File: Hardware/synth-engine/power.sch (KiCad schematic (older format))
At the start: 9 parts

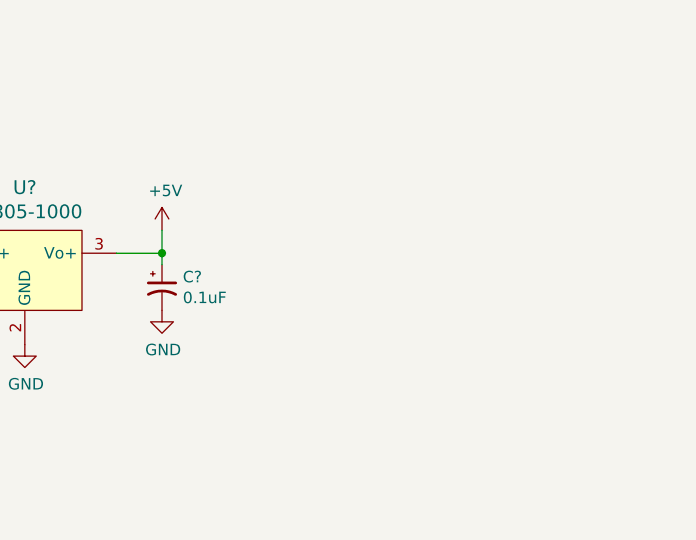
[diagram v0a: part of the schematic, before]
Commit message: add 3.3V voltage regulator
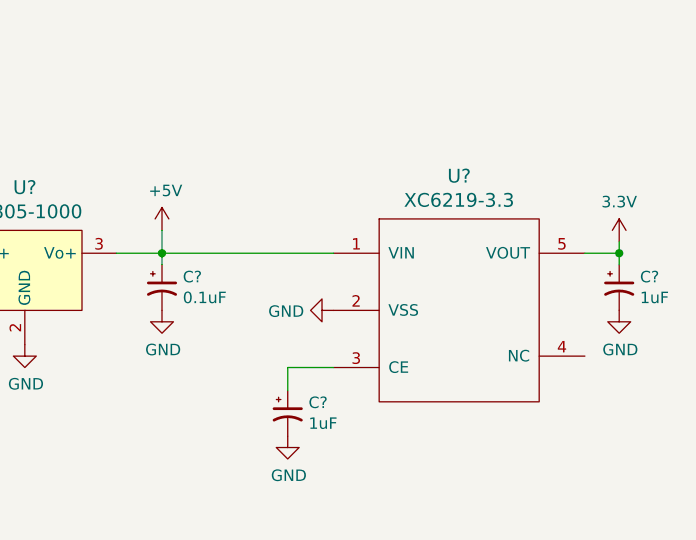
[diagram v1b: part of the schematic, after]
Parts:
- added C? (x2): 1uF, symbol Device:CP1_Small
- added U?: XC6219-3.3, symbol dac:XC6219-3.3
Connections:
- net +5V: now also U?.1 (VIN)
- net GND: now also C?.2, C?.2, U?.2 (VSS)
- new net: C?.1, U?.3 (CE)
- new net 3.3V: C?.1, U?.5 (VOUT)
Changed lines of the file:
@@
 	6150 2100 6150 2200
 Connection ~ 6150 2200
+$Comp
+L SparkFun-Aesthetics:3.3V #SUPPLY?
+U 1 1 5DD89EE3
+P 8150 2150
+F 0 "#SUPPLY?" H 8150 2150 50  0001 L BNN
+F 1 "3.3V" H 8150 2324 50  0000 C CNN
+F 2 "" H 8150 2150 50  0001 C CNN
+F 3 "" H 8150 2150 50  0001 C CNN
+	1    8150 2150
+	1    0    0    -1
+$EndComp
+$Comp
+L dac:XC6219-3.3 U?
+U 1 1 5DD89FB2
+P 7500 2450
+F 0 "U?" H 7450 3037 60  0000 C CNN
+F 1 "XC6219-3.3" H 7450 2931 60  0000 C CNN
+F 2 "" H 7500 2650 60  0000 C CNN
+F 3 "" H 7500 2650 60  0000 C CNN
+	1    7500 2450
+	1    0    0    -1
+$EndComp
+Wire Wire Line
+	6150 2200 6900 2200
+Wire Wire Line
+	8150 2150 8150 2200
+Wire Wire Line
+	8150 2200 8000 2200
+$Comp
+L Device:CP1_Small C?
+U 1 1 5DD8B50D
+P 6700 2900
+F 0 "C?" H 6791 2946 50  0000 L CNN
+F 1 "1uF" H 6791 2855 50  0000 L CNN
+F 2 "" H 6700 2900 50  0001 C CNN
+F 3 "~" H 6700 2900 50  0001 C CNN
+	1    6700 2900
+	1    0    0    -1
+$EndComp
+Wire Wire Line
+	6700 2800 6700 2700
+Wire Wire Line
+	6700 2700 6900 2700
+$Comp
+L power:GND #PWR?
+U 1 1 5DD8B762
+P 6700 3000
+F 0 "#PWR?" H 6700 2750 50  0001 C CNN
+F 1 "GND" H 6705 2827 50  0000 C CNN
+F 2 "" H 6700 3000 50  0001 C CNN
+F 3 "" H 6700 3000 50  0001 C CNN
+	1    6700 3000
+	1    0    0    -1
+$EndComp
+$Comp
+L power:GND #PWR?
+U 1 1 5DD8B7B9
+P 6900 2450
+F 0 "#PWR?" H 6900 2200 50  0001 C CNN
+F 1 "GND" V 6905 2322 50  0000 R CNN
+F 2 "" H 6900 2450 50  0001 C CNN
+F 3 "" H 6900 2450 50  0001 C CNN
+	1    6900 2450
+	0    1    1    0
+$EndComp
+$Comp
+L Device:CP1_Small C?
+U 1 1 5DD8B7E5
+P 8150 2350
+F 0 "C?" H 8241 2396 50  0000 L CNN
+F 1 "1uF" H 8241 2305 50  0000 L CNN
+F 2 "" H 8150 2350 50  0001 C CNN
+F 3 "~" H 8150 2350 50  0001 C CNN
+	1    8150 2350
+	1    0    0    -1
+$EndComp
+Wire Wire Line
+	8150 2250 8150 2200
+Connection ~ 8150 2200
+$Comp
+L power:GND #PWR?
+U 1 1 5DD8BD69
+P 8150 2450
+F 0 "#PWR?" H 8150 2200 50  0001 C CNN
+F 1 "GND" H 8155 2277 50  0000 C CNN
+F 2 "" H 8150 2450 50  0001 C CNN
+F 3 "" H 8150 2450 50  0001 C CNN
+	1    8150 2450
+	1    0    0    -1
+$EndComp
 $EndSCHEMATC

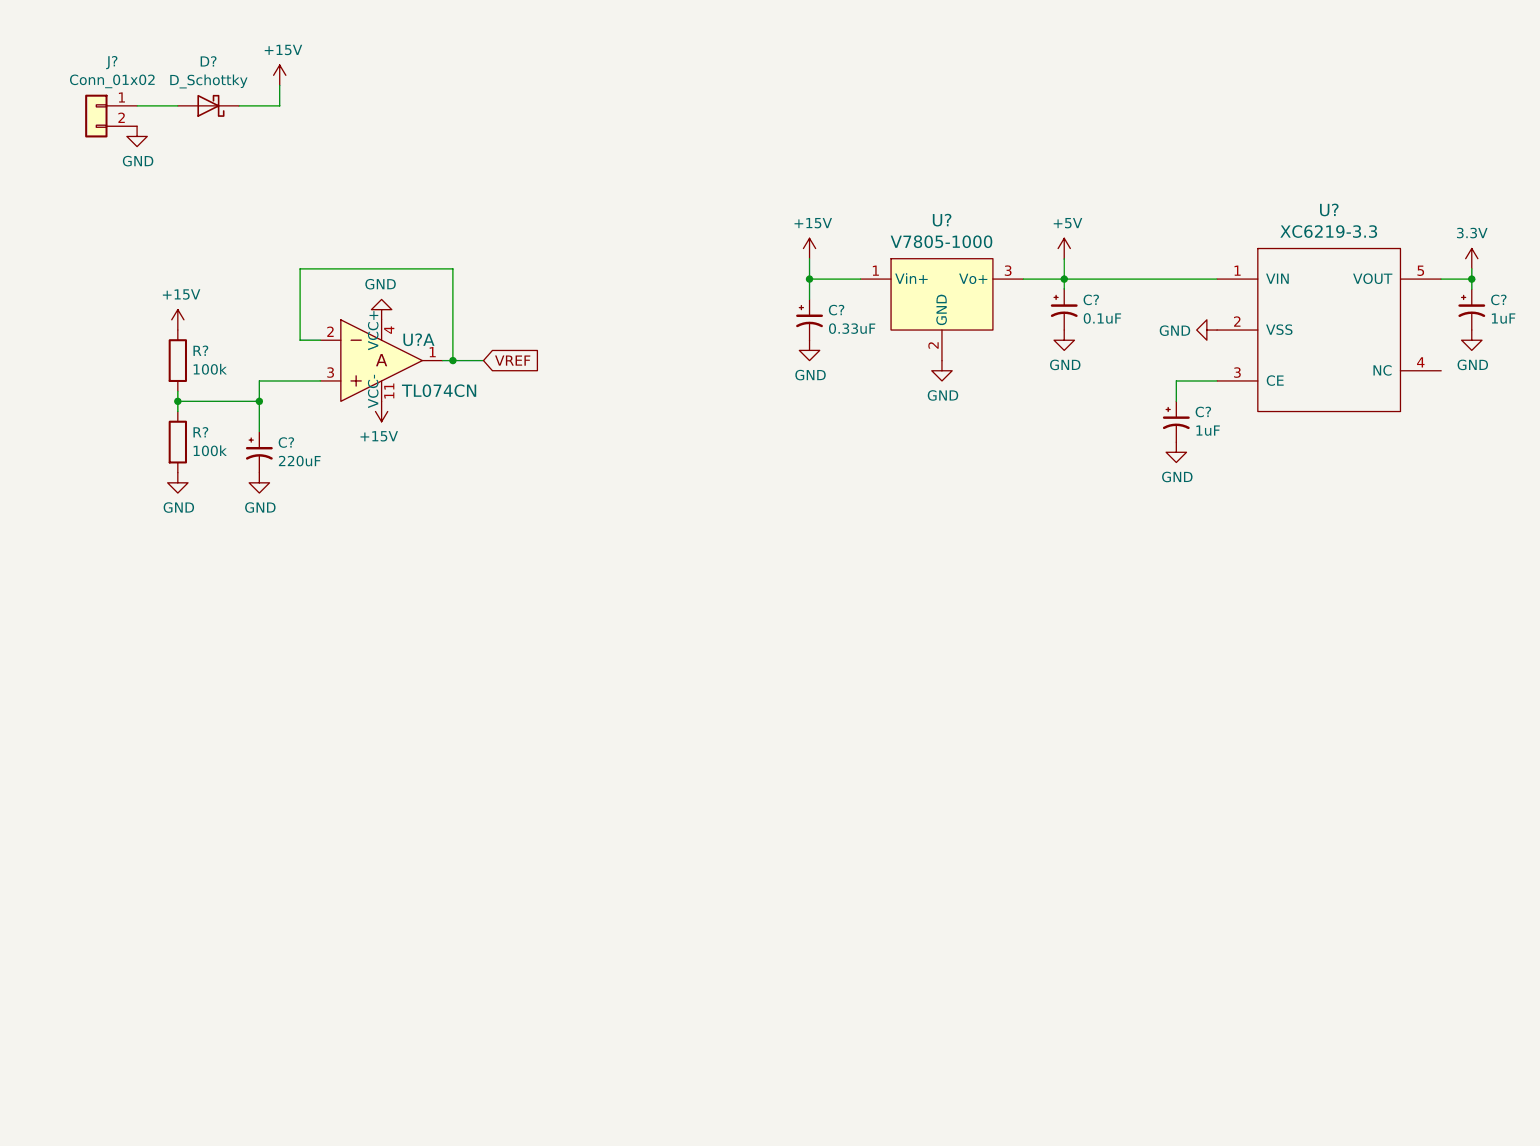
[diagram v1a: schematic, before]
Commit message: add 3.3V analog regulator and add power nets to AK4490
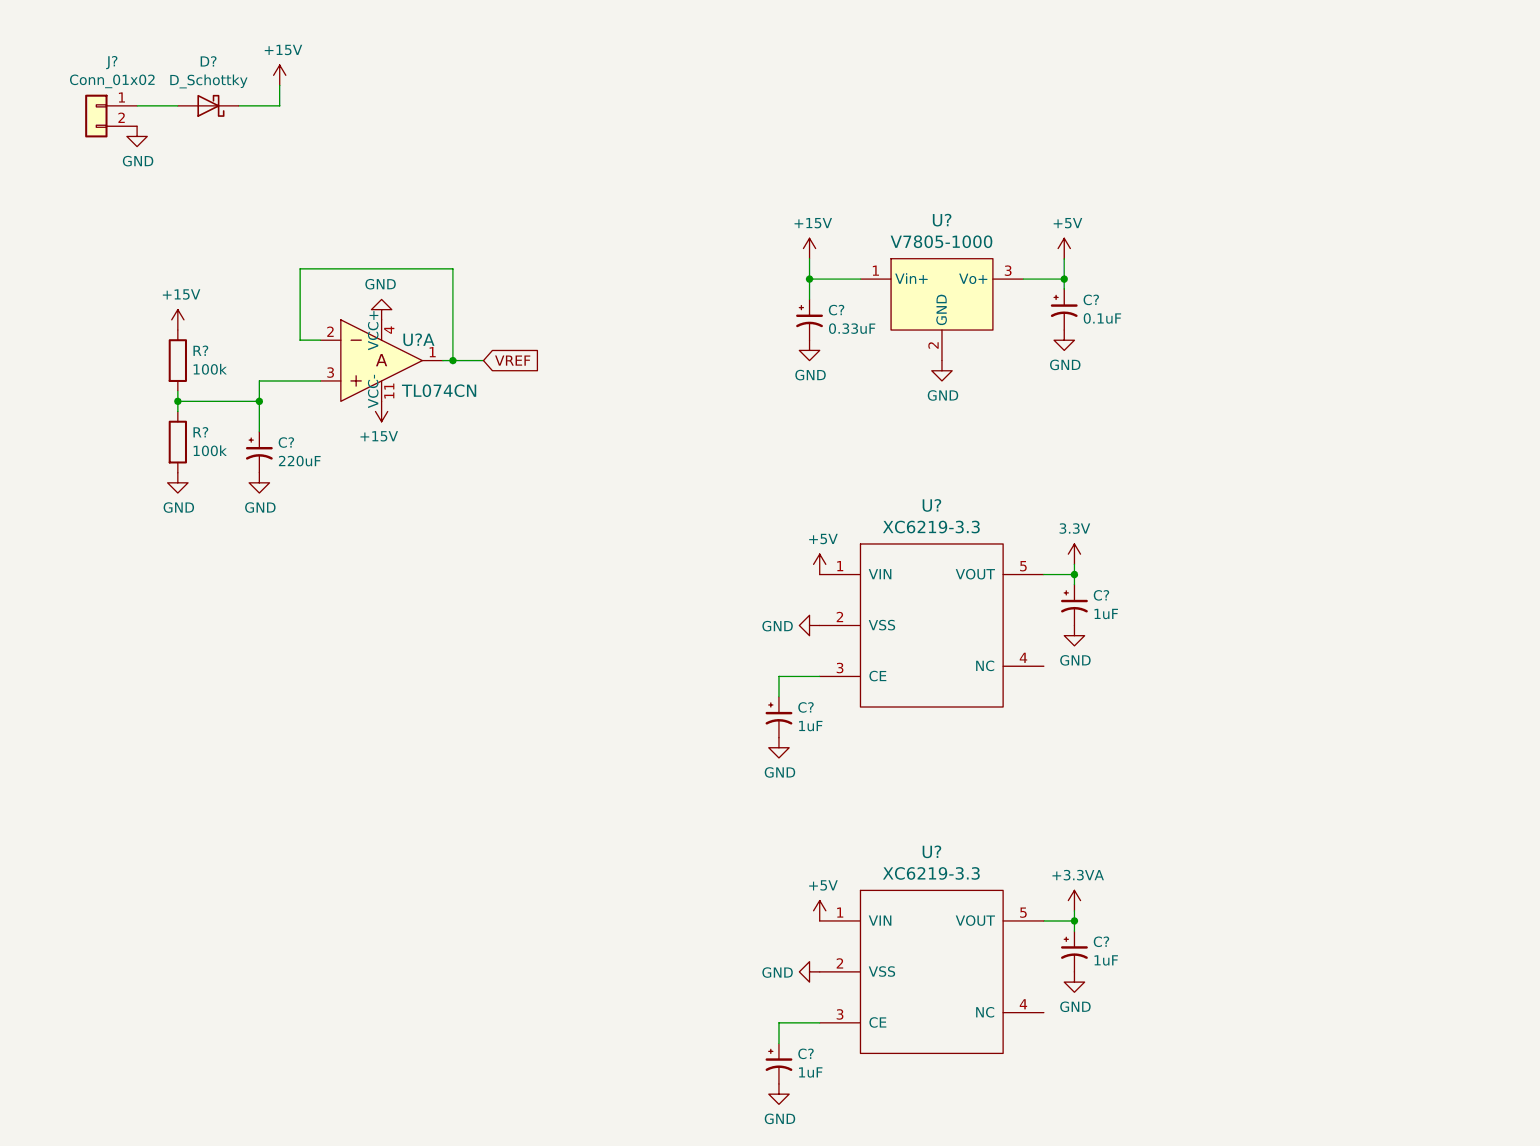
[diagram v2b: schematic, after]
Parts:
- added C? (x2): 1uF, symbol Device:CP1_Small
- added U?: XC6219-3.3, symbol dac:XC6219-3.3
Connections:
- net +5V: now also U?.1 (VIN)
- net GND: now also C?.2, C?.2, U?.2 (VSS)
- new net: C?.1, U?.3 (CE)
- new net +3.3VA: C?.1, U?.5 (VOUT)
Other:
- moved on the sheet: C?, U?
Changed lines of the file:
@@
 $Descr A4 11693 8268
 encoding utf-8
-Sheet 5 5
+Sheet 5 6
 Title ""
 Date ""
@@
 L SparkFun-Aesthetics:3.3V #SUPPLY?
 U 1 1 5DD89EE3
-P 8150 2150
-F 0 "#SUPPLY?" H 8150 2150 50  0001 L BNN
-F 1 "3.3V" H 8150 2324 50  0000 C CNN
-F 2 "" H 8150 2150 50  0001 C CNN
-F 3 "" H 8150 2150 50  0001 C CNN
-	1    8150 2150
+P 6200 3600
+F 0 "#SUPPLY?" H 6200 3600 50  0001 L BNN
+F 1 "3.3V" H 6200 3774 50  0000 C CNN
+F 2 "" H 6200 3600 50  0001 C CNN
+F 3 "" H 6200 3600 50  0001 C CNN
+	1    6200 3600
 	1    0    0    -1
 $EndComp
@@
 L dac:XC6219-3.3 U?
 U 1 1 5DD89FB2
-P 7500 2450
-F 0 "U?" H 7450 3037 60  0000 C CNN
-F 1 "XC6219-3.3" H 7450 2931 60  0000 C CNN
-F 2 "" H 7500 2650 60  0000 C CNN
-F 3 "" H 7500 2650 60  0000 C CNN
-	1    7500 2450
-	1    0    0    -1
-$EndComp
-Wire Wire Line
-	6150 2200 6900 2200
-Wire Wire Line
-	8150 2150 8150 2200
-Wire Wire Line
-	8150 2200 8000 2200
+P 5550 3900
+F 0 "U?" H 5500 4487 60  0000 C CNN
+F 1 "XC6219-3.3" H 5500 4381 60  0000 C CNN
+F 2 "" H 5550 4100 60  0000 C CNN
+F 3 "" H 5550 4100 60  0000 C CNN
+	1    5550 3900
+	1    0    0    -1
+$EndComp
+Wire Wire Line
+	6200 3600 6200 3650
+Wire Wire Line
+	6200 3650 6050 3650
 $Comp
 L Device:CP1_Small C?
 U 1 1 5DD8B50D
-P 6700 2900
-F 0 "C?" H 6791 2946 50  0000 L CNN
-F 1 "1uF" H 6791 2855 50  0000 L CNN
-F 2 "" H 6700 2900 50  0001 C CNN
-F 3 "~" H 6700 2900 50  0001 C CNN
-	1    6700 2900
-	1    0    0    -1
-$EndComp
-Wire Wire Line
-	6700 2800 6700 2700
-Wire Wire Line
-	6700 2700 6900 2700
+P 4750 4350
+F 0 "C?" H 4841 4396 50  0000 L CNN
+F 1 "1uF" H 4841 4305 50  0000 L CNN
+F 2 "" H 4750 4350 50  0001 C CNN
+F 3 "~" H 4750 4350 50  0001 C CNN
+	1    4750 4350
+	1    0    0    -1
+$EndComp
+Wire Wire Line
+	4750 4250 4750 4150
+Wire Wire Line
+	4750 4150 4950 4150
 $Comp
 L power:GND #PWR?
 U 1 1 5DD8B762
-P 6700 3000
-F 0 "#PWR?" H 6700 2750 50  0001 C CNN
-F 1 "GND" H 6705 2827 50  0000 C CNN
-F 2 "" H 6700 3000 50  0001 C CNN
-F 3 "" H 6700 3000 50  0001 C CNN
-	1    6700 3000
+P 4750 4450
+F 0 "#PWR?" H 4750 4200 50  0001 C CNN
+F 1 "GND" H 4755 4277 50  0000 C CNN
+F 2 "" H 4750 4450 50  0001 C CNN
+F 3 "" H 4750 4450 50  0001 C CNN
+	1    4750 4450
 	1    0    0    -1
 $EndComp
@@
 L power:GND #PWR?
 U 1 1 5DD8B7B9
-P 6900 2450
-F 0 "#PWR?" H 6900 2200 50  0001 C CNN
-F 1 "GND" V 6905 2322 50  0000 R CNN
-F 2 "" H 6900 2450 50  0001 C CNN
-F 3 "" H 6900 2450 50  0001 C CNN
-	1    6900 2450
+P 4950 3900
+F 0 "#PWR?" H 4950 3650 50  0001 C CNN
+F 1 "GND" V 4955 3772 50  0000 R CNN
+F 2 "" H 4950 3900 50  0001 C CNN
+F 3 "" H 4950 3900 50  0001 C CNN
+	1    4950 3900
 	0    1    1    0
 $EndComp
@@
 L Device:CP1_Small C?
 U 1 1 5DD8B7E5
-P 8150 2350
-F 0 "C?" H 8241 2396 50  0000 L CNN
-F 1 "1uF" H 8241 2305 50  0000 L CNN
-F 2 "" H 8150 2350 50  0001 C CNN
-F 3 "~" H 8150 2350 50  0001 C CNN
-	1    8150 2350
-	1    0    0    -1
-$EndComp
-Wire Wire Line
-	8150 2250 8150 2200
-Connection ~ 8150 2200
+P 6200 3800
+F 0 "C?" H 6291 3846 50  0000 L CNN
+F 1 "1uF" H 6291 3755 50  0000 L CNN
+F 2 "" H 6200 3800 50  0001 C CNN
+F 3 "~" H 6200 3800 50  0001 C CNN
+	1    6200 3800
+	1    0    0    -1
+$EndComp
+Wire Wire Line
+	6200 3700 6200 3650
+Connection ~ 6200 3650
 $Comp
 L power:GND #PWR?
 U 1 1 5DD8BD69
-P 8150 2450
-F 0 "#PWR?" H 8150 2200 50  0001 C CNN
-F 1 "GND" H 8155 2277 50  0000 C CNN
-F 2 "" H 8150 2450 50  0001 C CNN
-F 3 "" H 8150 2450 50  0001 C CNN
-	1    8150 2450
-	1    0    0    -1
-$EndComp
+P 6200 3900
+F 0 "#PWR?" H 6200 3650 50  0001 C CNN
+F 1 "GND" H 6205 3727 50  0000 C CNN
+F 2 "" H 6200 3900 50  0001 C CNN
+F 3 "" H 6200 3900 50  0001 C CNN
+	1    6200 3900
+	1    0    0    -1
+$EndComp
+$Comp
+L power:+5V #PWR?
+U 1 1 5DD603B6
+P 4950 3650
+F 0 "#PWR?" H 4950 3500 50  0001 C CNN
+F 1 "+5V" H 4965 3823 50  0000 C CNN
+F 2 "" H 4950 3650 50  0001 C CNN
+F 3 "" H 4950 3650 50  0001 C CNN
+	1    4950 3650
+	1    0    0    -1
+$EndComp
+$Comp
+L dac:XC6219-3.3 U?
+U 1 1 5DD60943
+P 5550 5600
+F 0 "U?" H 5500 6187 60  0000 C CNN
+F 1 "XC6219-3.3" H 5500 6081 60  0000 C CNN
+F 2 "" H 5550 5800 60  0000 C CNN
+F 3 "" H 5550 5800 60  0000 C CNN
+	1    5550 5600
+	1    0    0    -1
+$EndComp
+Wire Wire Line
+	6200 5300 6200 5350
+Wire Wire Line
+	6200 5350 6050 5350
+$Comp
+L Device:CP1_Small C?
+U 1 1 5DD6094B
+P 4750 6050
+F 0 "C?" H 4841 6096 50  0000 L CNN
+F 1 "1uF" H 4841 6005 50  0000 L CNN
+F 2 "" H 4750 6050 50  0001 C CNN
+F 3 "~" H 4750 6050 50  0001 C CNN
+	1    4750 6050
+	1    0    0    -1
+$EndComp
+Wire Wire Line
+	4750 5950 4750 5850
+Wire Wire Line
+	4750 5850 4950 5850
+$Comp
+L power:GND #PWR?
+U 1 1 5DD60953
+P 4750 6150
+F 0 "#PWR?" H 4750 5900 50  0001 C CNN
+F 1 "GND" H 4755 5977 50  0000 C CNN
+F 2 "" H 4750 6150 50  0001 C CNN
+F 3 "" H 4750 6150 50  0001 C CNN
+	1    4750 6150
+	1    0    0    -1
+$EndComp
+$Comp
+L power:GND #PWR?
+U 1 1 5DD60959
+P 4950 5600
+F 0 "#PWR?" H 4950 5350 50  0001 C CNN
+F 1 "GND" V 4955 5472 50  0000 R CNN
+F 2 "" H 4950 5600 50  0001 C CNN
+F 3 "" H 4950 5600 50  0001 C CNN
+	1    4950 5600
+	0    1    1    0
+$EndComp
+$Comp
+L Device:CP1_Small C?
+U 1 1 5DD6095F
+P 6200 5500
+F 0 "C?" H 6291 5546 50  0000 L CNN
+F 1 "1uF" H 6291 5455 50  0000 L CNN
+F 2 "" H 6200 5500 50  0001 C CNN
+F 3 "~" H 6200 5500 50  0001 C CNN
+	1    6200 5500
+	1    0    0    -1
+$EndComp
+Wire Wire Line
+	6200 5400 6200 5350
+Connection ~ 6200 5350
+$Comp
+L power:GND #PWR?
+U 1 1 5DD60967
+P 6200 5600
+F 0 "#PWR?" H 6200 5350 50  0001 C CNN
+F 1 "GND" H 6205 5427 50  0000 C CNN
+F 2 "" H 6200 5600 50  0001 C CNN
+F 3 "" H 6200 5600 50  0001 C CNN
+	1    6200 5600
+	1    0    0    -1
+$EndComp
+$Comp
+L power:+5V #PWR?
+U 1 1 5DD6096D
+P 4950 5350
+F 0 "#PWR?" H 4950 5200 50  0001 C CNN
+F 1 "+5V" H 4965 5523 50  0000 C CNN
+F 2 "" H 4950 5350 50  0001 C CNN
+F 3 "" H 4950 5350 50  0001 C CNN
+	1    4950 5350
+	1    0    0    -1
+$EndComp
+$Comp
+L power:+3.3VA #PWR?
+U 1 1 5DD60F1E
+P 6200 5300
+F 0 "#PWR?" H 6200 5150 50  0001 C CNN
+F 1 "+3.3VA" H 6215 5473 50  0000 C CNN
+F 2 "" H 6200 5300 50  0001 C CNN
+F 3 "" H 6200 5300 50  0001 C CNN
+	1    6200 5300
+	1    0    0    -1
+$EndComp

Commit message: add filtering in front of 3.3V regulators
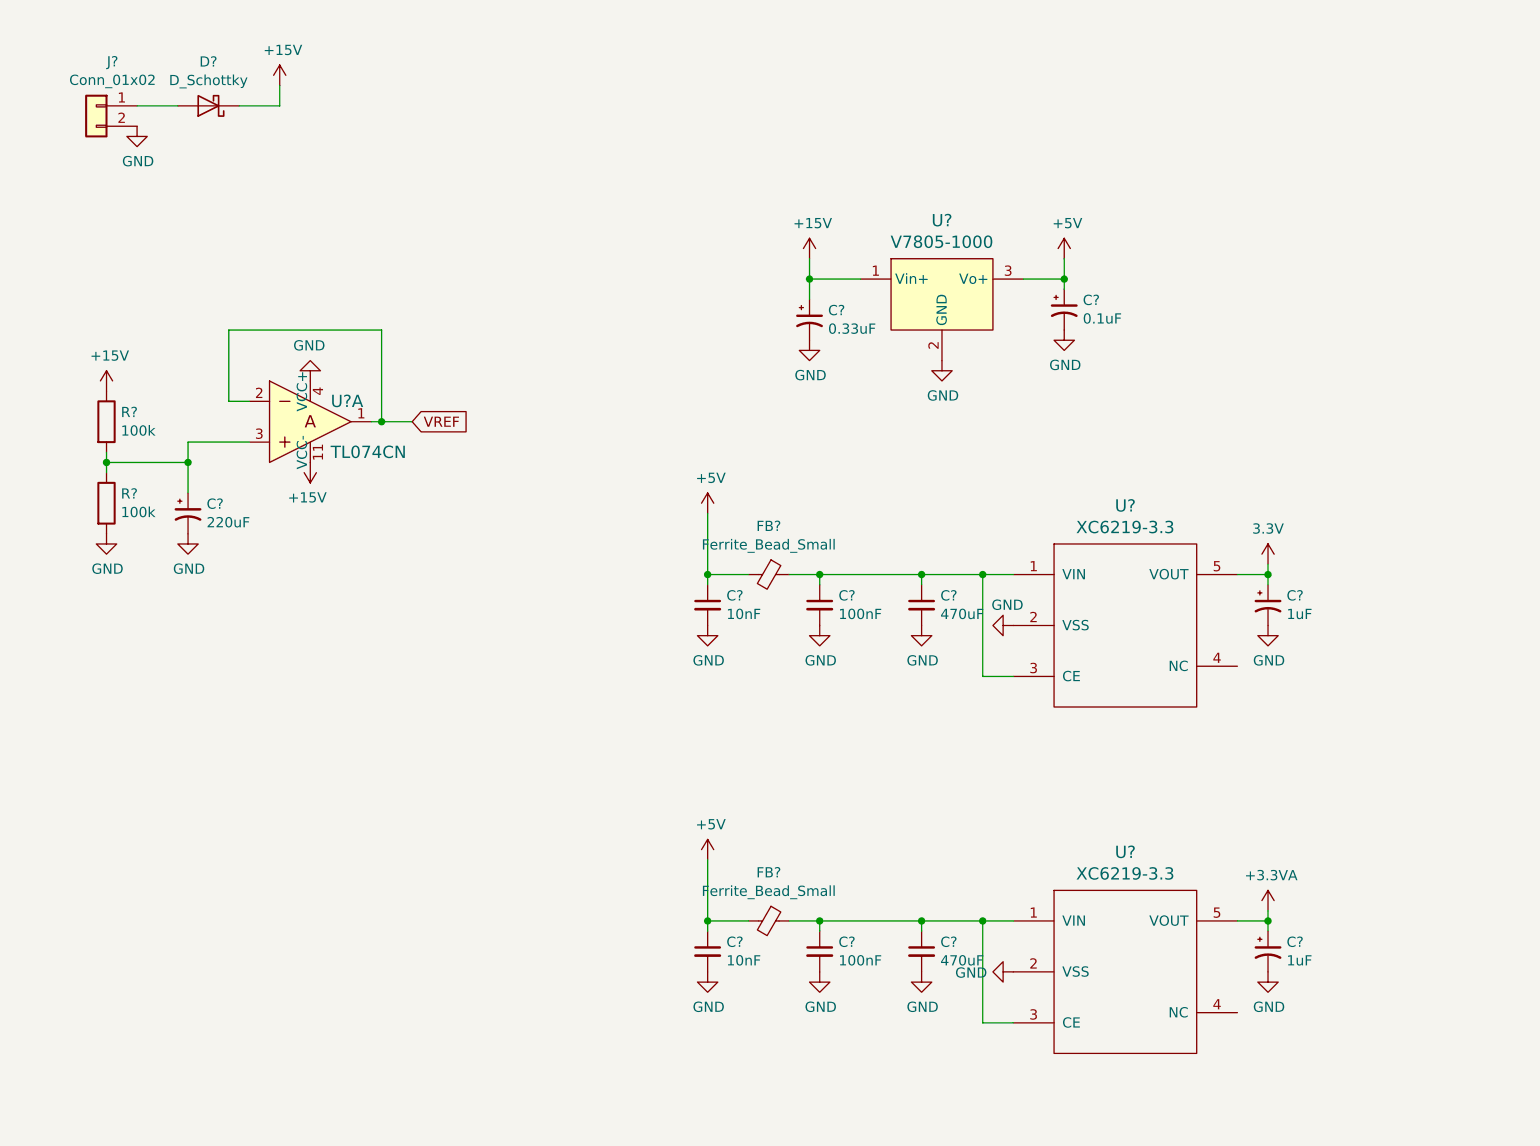
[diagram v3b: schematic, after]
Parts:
- removed C? (x2): 1uF, symbol Device:CP1_Small
- added C? (x2): 10nF, symbol Device:C_Small
- added C? (x2): 100nF, symbol Device:C_Small
- added C? (x2): 470uF, symbol Device:C_Small
- added FB? (x2): Ferrite_Bead_Small, symbol Device:Ferrite_Bead_Small
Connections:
- net +5V: now also C?.1, C?.1, FB?.2, FB?.2; no longer U?.1 (VIN), U?.1 (VIN)
- net GND: now also C?.2, C?.2, C?.2, C?.2, C?.2, C?.2
- net at U?.3 (CE): now also U?.1 (VIN), C?.1, C?.1, FB?.1 (x2)
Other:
- moved on the sheet: C?, R?, U?, U?A
